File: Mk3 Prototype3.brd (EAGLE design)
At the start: 121.6 x 70 mm, 152 parts, among them IC1 TPD3E001DRL, IC2 TPS62082, IC3 STM32F401V, IC4 BQ24092, IC6 CC3100MOD, IC7 BQ2970, IC8 LSM6DS3, IC9 LIS3MDL, J1 ZX62-AB-5PA(11), J2 ER-CON50HT-1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

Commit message: updating usd
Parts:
- U1: value USD-SOCKET-SDIODM3AT_0011 -> USD-SOCKET-SDIO; device TiLDA Mk3 Parts:DM3AT_0011 -> TiLDA Mk3 Parts:0011XAAX09X
- moved R5 0.80 mm to (24.2, 3.40)
- moved U1 0.40 mm to (6.80, 35.6)
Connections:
- net GND: no longer U1.GND4, U1.GND5, U1.GND6, U1.GND7
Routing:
- net GND: track 159.8 -> 160.4 mm, vias 157 -> 158

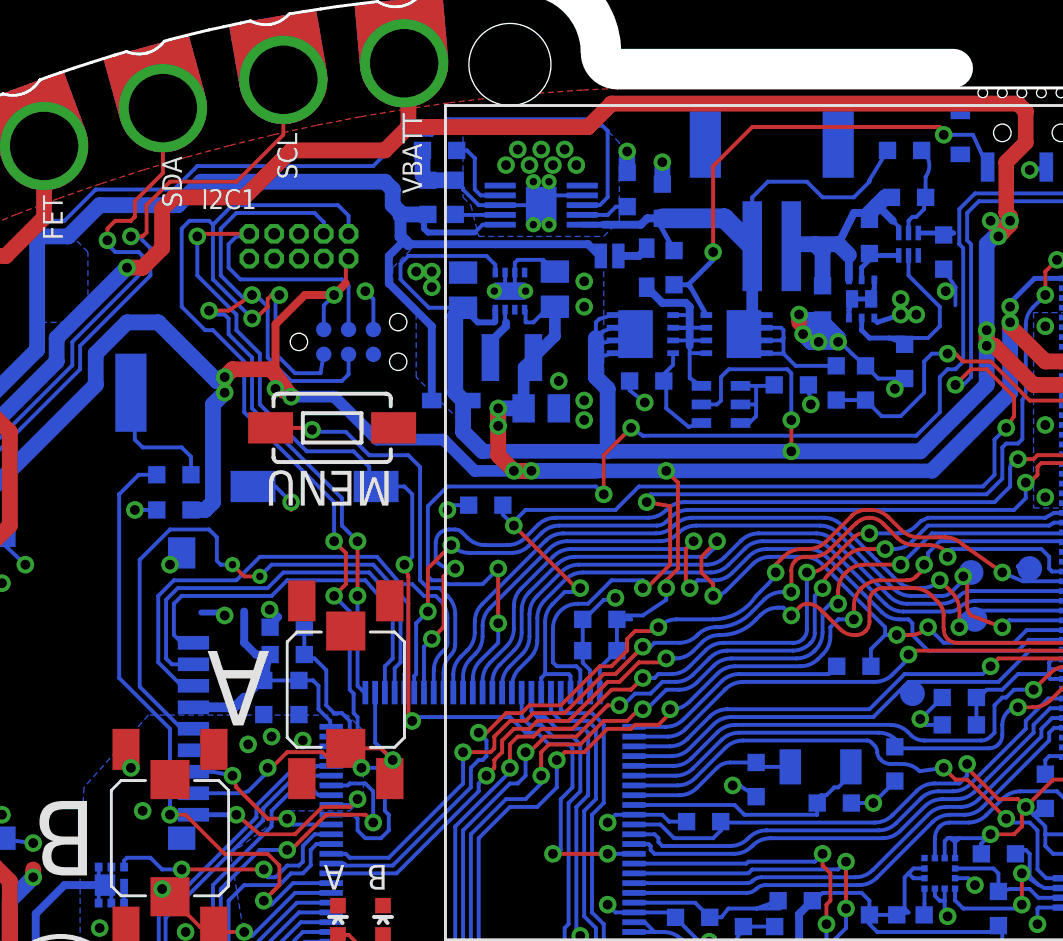
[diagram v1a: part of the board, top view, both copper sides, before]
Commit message: changing out diodes
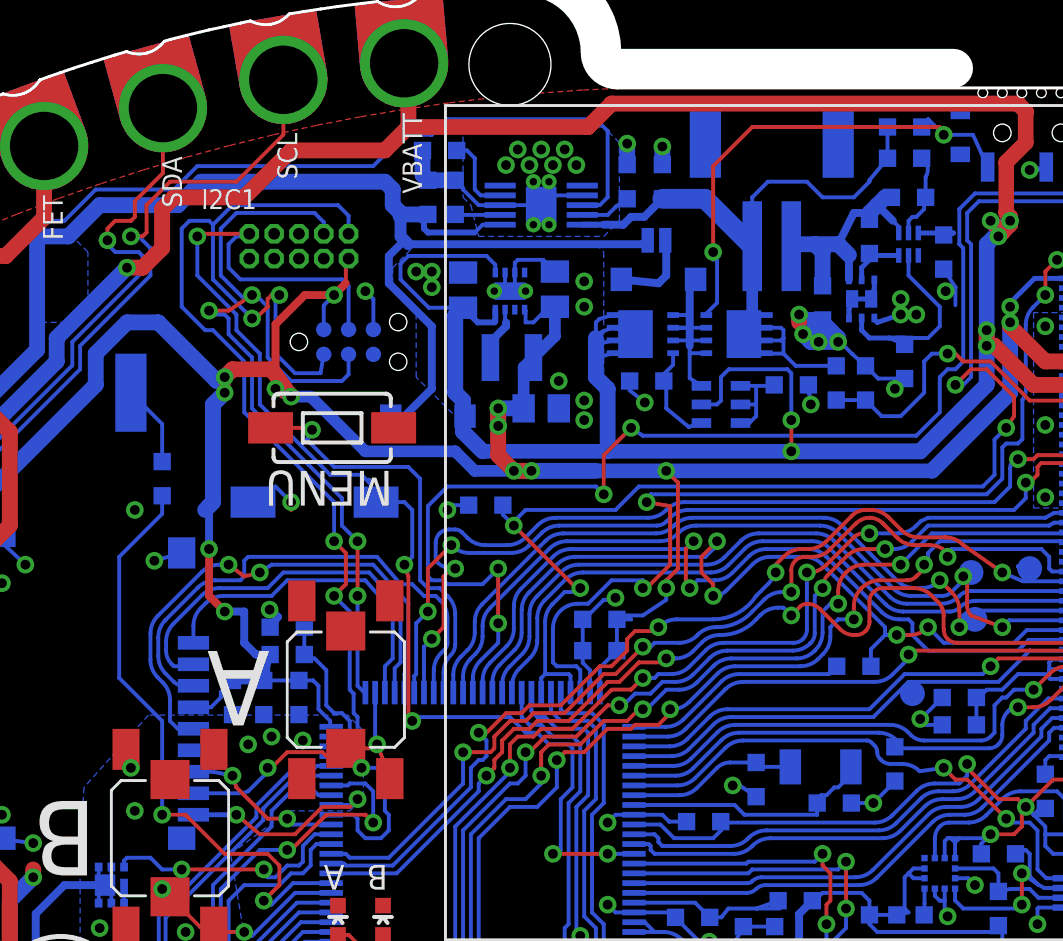
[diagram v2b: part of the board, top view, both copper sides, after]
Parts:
- D2, D3: value (none) -> NTS245SFT1G; device TiLDA Mk3 Parts:SOD-323F -> Diodes:SOD123
- moved R45 13.8 mm to (53.8, 61.2), turned to 180 degrees
- moved C17 10.1 mm to (19.4, 32.0), turned to 90 degrees
- moved SJ1 2.53 mm to (41.1, 55.4)
- moved D3 1.44 mm to (29.4, 46.4), turned to 0 degrees
- moved C3 1.00 mm to (41.4, 58.4)
- moved D2 0.85 mm to (41.2, 53.4), turned to 180 degrees
- moved S1 0.80 mm to (23.6, 42.0)
- moved R26 0.63 mm to (15.8, 43.2), turned to 270 degrees
- moved R13 0.40 mm to (39.6, 58.4)
- moved R51 0.40 mm to (53.8, 59.6)
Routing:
- net +3V3: track 588.8 -> 594.0 mm, vias 33 -> 35
- net SDIO_CLK: track 32.0 -> 27.2 mm
- net VBUS: track 127.2 -> 131.9 mm
- net N$28: track 1.62 -> 4.28 mm
- net N$4: track 6.65 -> 4.19 mm
- net SDIO_D2: track 19.5 -> 17.2 mm
- net GND: track 160.4 -> 158.2 mm, vias 158 -> 157
- net BUZZ: track 32.9 -> 31.7 mm
- net N$16: track 14.6 -> 13.4 mm
- net SDIO_D3: track 22.4 -> 21.3 mm
- net N$54: track 25.4 -> 26.2 mm
- net V_UNREG: track 347.7 -> 348.5 mm
- net BTN_A: track 8.01 -> 7.26 mm
- net SDIO_CMD: track 26.9 -> 26.3 mm
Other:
- board text added: "Tilda Mk3 Rev.3 May 2016"
- board text removed: "Tilda Mk3 Rev.2 Apr 2016"

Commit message: no overlap
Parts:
- moved SW1 0.70 mm to (97.1, 28.9)
- moved R5 0.40 mm to (24.6, 3.40)
- moved LED5 0.20 mm to (21.4, 6.10)
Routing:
- net +3V3: track 594.0 -> 546.7 mm, vias 35 -> 33
- net GND: track 158.2 -> 143.3 mm, vias 157 -> 156
- net SDIO_D1: track 18.2 -> 24.0 mm
- net I2C_SCL: track 159.5 -> 156.7 mm
- net V_UNREG: track 348.5 -> 351.1 mm
- net CC_HIB: track 130.2 -> 128.1 mm
- net NRST: track 64.6 -> 62.7 mm
- net TIM1_CH1N: track 12.9 -> 14.4 mm
- net JOY_RIGHT: track 144.6 -> 146.0 mm
- net I2C_SDA: track 157.4 -> 156.3 mm
- net TIM1_CH2: track 20.9 -> 19.8 mm
- net CC_RST: track 119.3 -> 118.2 mm
- net N$29: track 10.7 -> 9.76 mm
- net N$63: track 2.31 -> 1.34 mm
- net BTN_A: track 7.26 -> 8.15 mm
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- removed copper zone on layer 16, net FET_OUT

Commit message: routing done
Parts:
- removed R24: 0603/330/5%, TiLDA Mk3 Parts:C0603K-SMALL
- added TP4: TPB1,27, TiLDA Mk3 Parts:B1,27
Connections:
- removed net SPI3_SCK: IC3.89, J2.37, R24.1
- net FSMC_A23: now also IC3.89, J2.37, TP4.TP; no longer R24.2
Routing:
- net FSMC_A23: track 11.5 -> 55.2 mm, vias 0 -> 4
- net SPI3_SCK: track 43.6 -> 0.00 mm, vias 4 -> 0

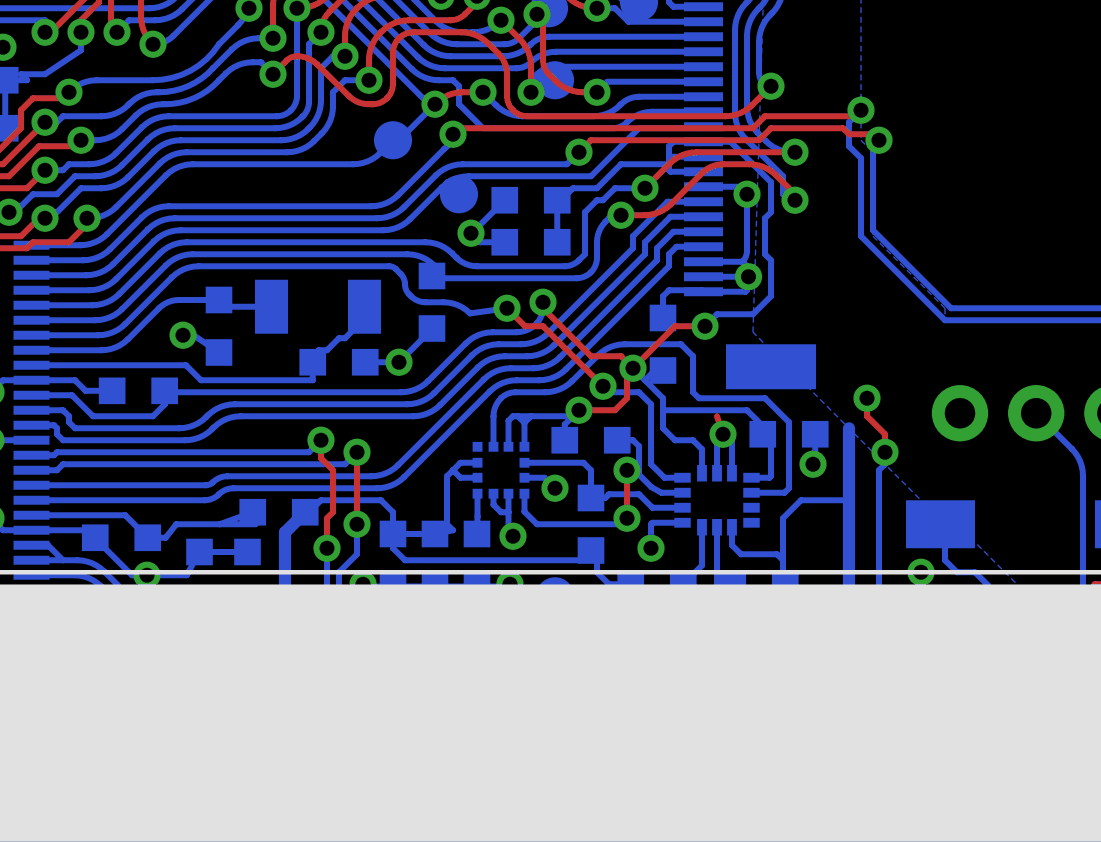
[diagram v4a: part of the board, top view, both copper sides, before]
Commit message: some silk cleanup
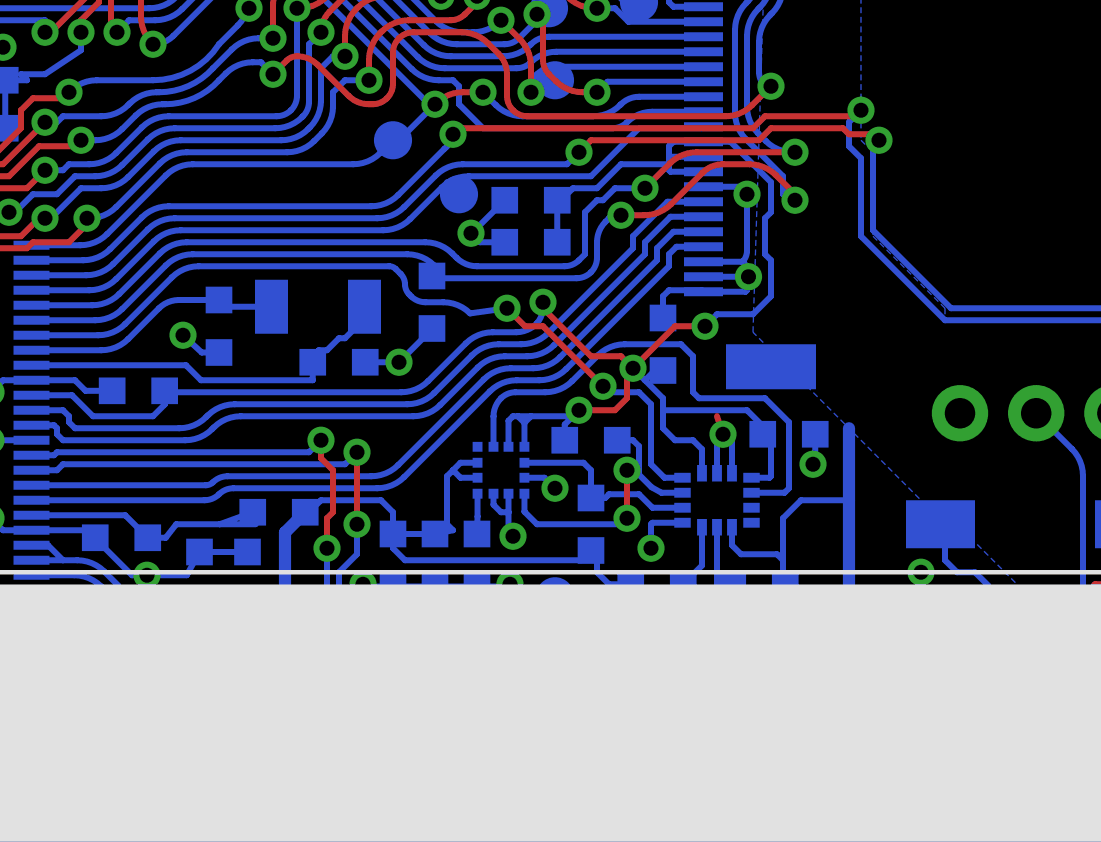
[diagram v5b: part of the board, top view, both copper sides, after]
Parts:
- removed LOGO2: MICROPYTHON-SILK, TiLDA Mk3 Parts:UPYTHON_LOGO_SLIKONLY
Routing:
- net ADC_VIN: track 60.0 -> 50.0 mm, vias 4 -> 2
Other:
- board text added: "A0"
- board text added: "D0"
- board text added: "DAC"
- board text added: "RD"
- board text added: "TEAR"
- board text added: "WR"

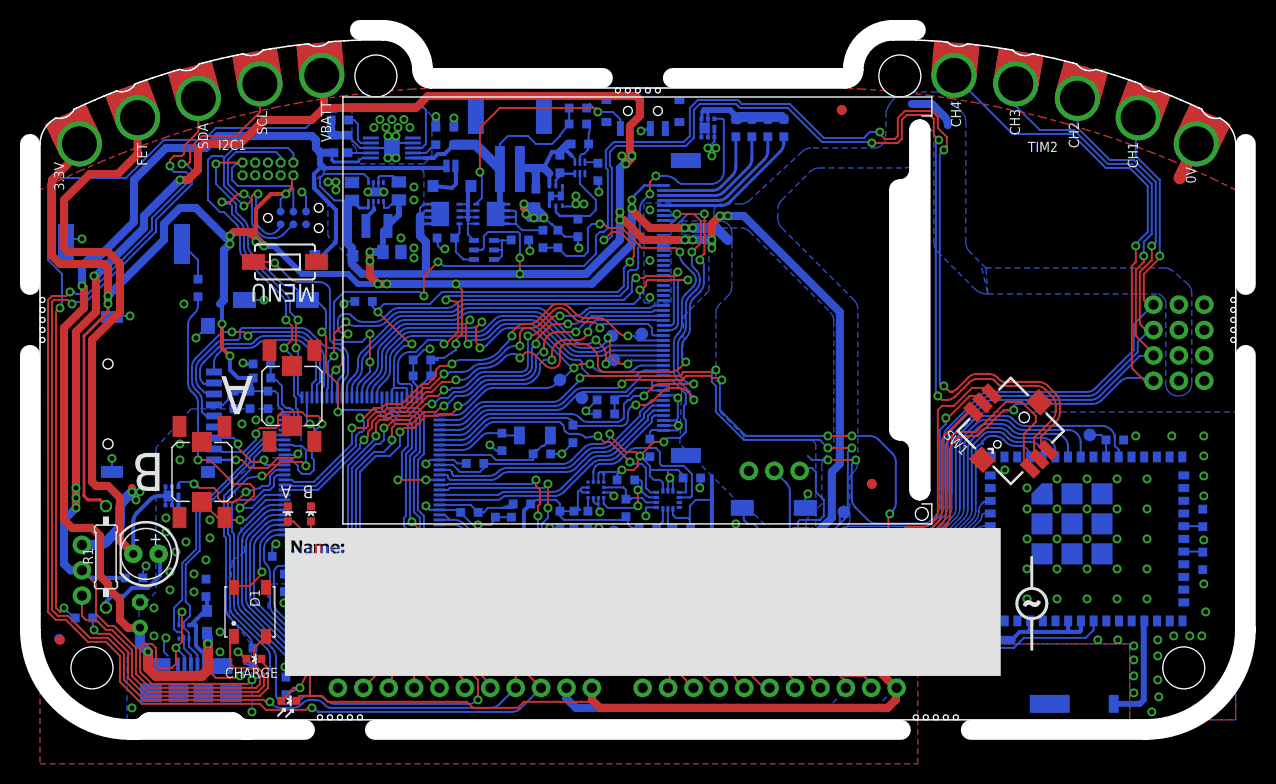
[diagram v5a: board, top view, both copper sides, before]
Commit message: Angle and clearance tidy
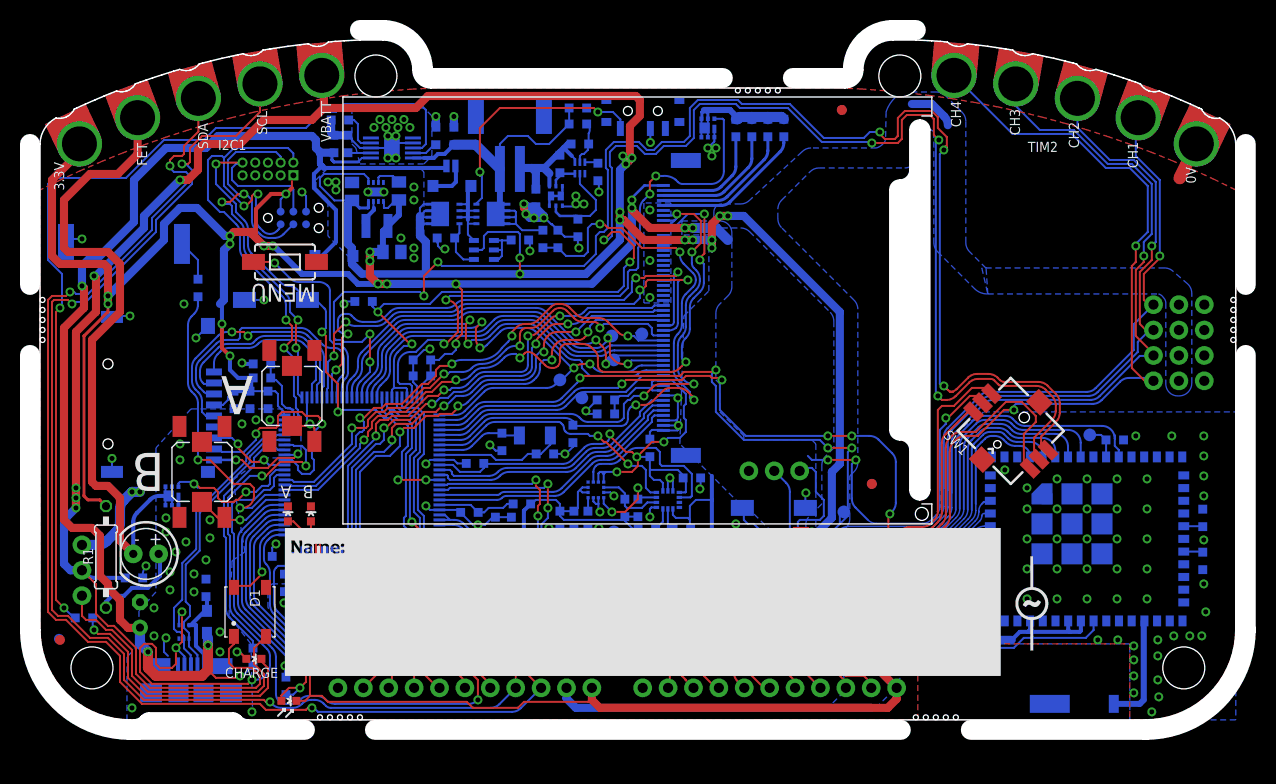
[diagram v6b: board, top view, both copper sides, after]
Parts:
- J3: value SWD_SHROUD -> SWD_SHROUD-PINHEAD; device dtb:SWD_PTH_SHROUD -> TiLDA Mk3 Parts:PINHEAD_2X05_127
- moved R31 3.05 mm to (59.8, 21.2), turned to 90 degrees
- moved C24 0.30 mm to (50.5, 26.6)
- moved R3 0.20 mm to (70.8, 17.6)
- moved R18 0.14 mm to (60.7, 19.1)
- moved R30 0.10 mm to (58.5, 21.2)
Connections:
- net N$26 renamed SDX
- net N$29 renamed SCX
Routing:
- net GND: track 143.1 -> 140.7 mm, vias 156 -> 155
- net +3V3: track 546.7 -> 544.9 mm
- net N$5: track 9.18 -> 8.04 mm
- net N$9: track 92.3 -> 91.5 mm
- net BOOT0: track 146.6 -> 147.3 mm
- net VBUS: track 131.2 -> 130.5 mm
- net SCX: track 9.76 -> 9.06 mm
- net WS2812: track 10.2 -> 9.52 mm
- net PB2: track 64.0 -> 63.4 mm
- net TIM17_CH1: track 61.8 -> 61.2 mm
- net JOY_RIGHT: track 146.0 -> 146.6 mm
- net N$60: track 9.88 -> 9.31 mm
- net ADC_LIGHT: track 23.0 -> 23.5 mm
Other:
- outline, holes or cut-outs redrawn
